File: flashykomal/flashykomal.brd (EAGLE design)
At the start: 54.6 x 58.4 mm, 29 parts, among them IC1 MEGA8-P, IC2 LM358, IC3 LM2397

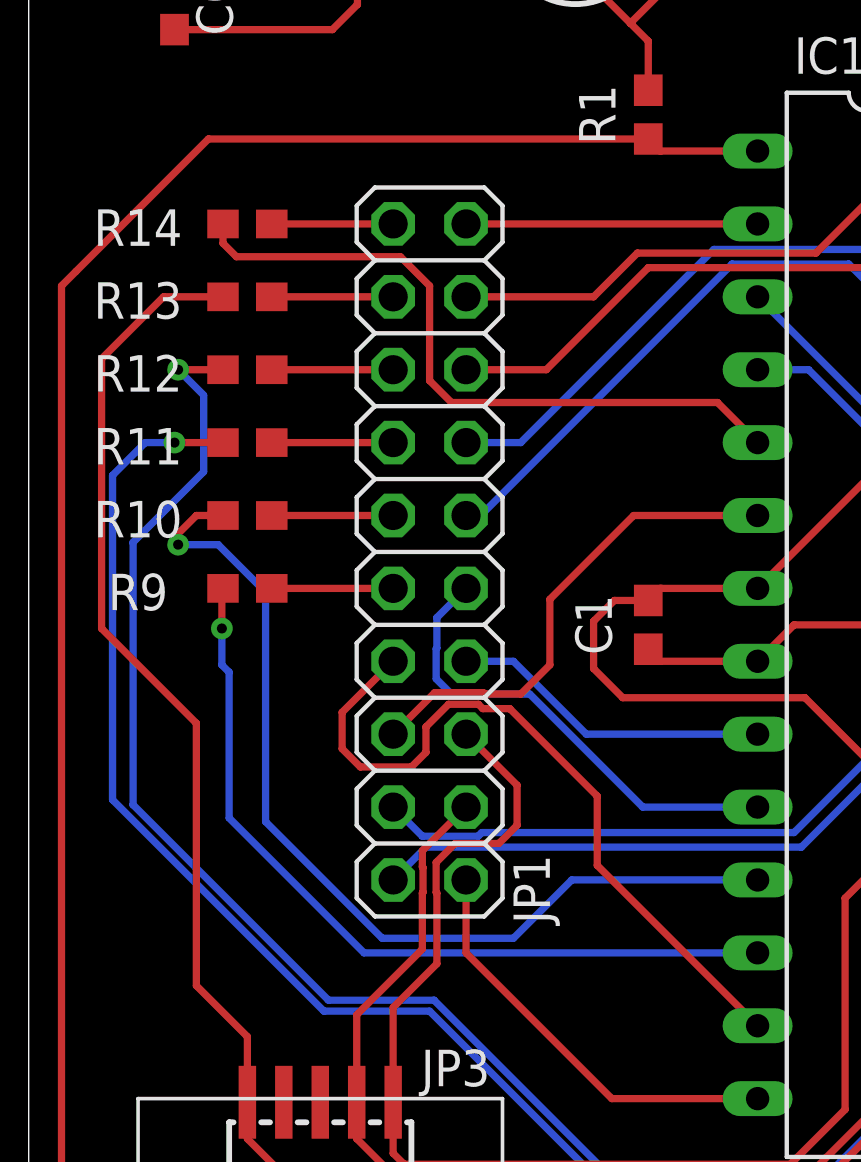
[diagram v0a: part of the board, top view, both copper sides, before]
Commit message: Add JP1 markings
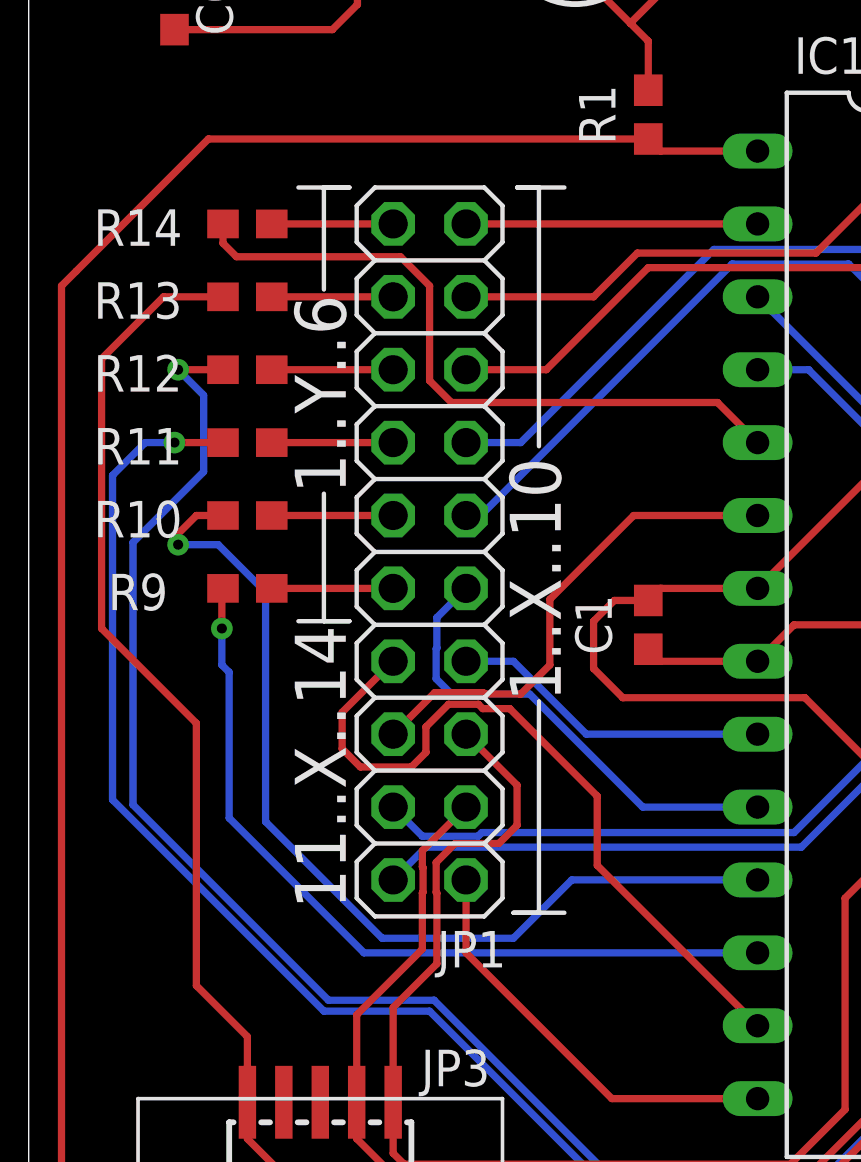
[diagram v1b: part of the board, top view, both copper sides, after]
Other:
- board text added: "1..X..10"
- board text added: "1..Y..6"
- board text added: "11..X..14"
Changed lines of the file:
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@@
 <?xml version="1.0" encoding="utf-8"?>
 <!DOCTYPE eagle SYSTEM "eagle.dtd">
-<eagle version="9.4.2">
+<eagle version="9.1.3">
 <drawing>
 <settings>
@@
 <text x="24.13" y="48.26" size="1.27" layer="25" ratio="15">VIN</text>
 <text x="31.75" y="48.26" size="1.27" layer="25" ratio="15">GND</text>
+<text x="18.542" y="22.733" size="1.778" layer="25" rot="R90">1..X..10</text>
+<text x="11.049" y="15.494" size="1.778" layer="25" rot="R90">11..X..14</text>
+<text x="11.049" y="29.972" size="1.778" layer="25" rot="R90">1..Y..6</text>
+<wire x1="10.287" y1="29.972" x2="10.287" y2="25.527" width="0.1524" layer="25"/>
+<wire x1="10.287" y1="25.527" x2="11.176" y2="25.527" width="0.1524" layer="25"/>
+<wire x1="11.176" y1="25.527" x2="9.398" y2="25.527" width="0.1524" layer="25"/>
+<wire x1="10.287" y1="37.084" x2="10.287" y2="40.64" width="0.1524" layer="25"/>
+<wire x1="10.287" y1="40.64" x2="11.176" y2="40.64" width="0.1524" layer="25"/>
+<wire x1="11.176" y1="40.64" x2="9.398" y2="40.64" width="0.1524" layer="25"/>
+<wire x1="17.78" y1="31.623" x2="17.78" y2="40.64" width="0.1524" layer="25"/>
+<wire x1="17.78" y1="40.64" x2="17.018" y2="40.64" width="0.1524" layer="25"/>
+<wire x1="17.018" y1="40.64" x2="18.669" y2="40.64" width="0.1524" layer="25"/>
+<wire x1="17.78" y1="22.733" x2="17.78" y2="15.367" width="0.1524" layer="25"/>
+<wire x1="17.78" y1="15.367" x2="16.891" y2="15.367" width="0.1524" layer="25"/>
+<wire x1="16.891" y1="15.367" x2="18.669" y2="15.367" width="0.1524" layer="25"/>
 </plain>
 <attributes>
@@
 </element>
 <element name="JP1" library="pinhead" library_urn="urn:adsk.eagle:library:325" package="2X10" package3d_urn="urn:adsk.eagle:package:22405/2" value="" x="13.97" y="27.94" smashed="yes" rot="R90">
-<attribute name="NAME" x="18.161" y="14.986" size="1.27" layer="25" ratio="10" rot="R90"/>
+<attribute name="NAME" x="16.637" y="14.732" size="1.27" layer="25" ratio="10" rot="R180"/>
 <attribute name="VALUE" x="18.415" y="15.24" size="1.27" layer="27" rot="R90"/>
 </element>

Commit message: Power LED
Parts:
- added D1: (no value), SparkFun-LED:LED-0603
- added R15: 330, SparkFun-Resistors:0603
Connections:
- new net N$1: D1.C, R15.2
- net GND: now also R15.1
- net VCC: now also D1.A, JP4.P$2
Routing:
- net VCC: track 151.3 -> 174.7 mm
- net N$1: track 0.00 -> 2.57 mm
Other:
- board text added: "PWR"
- board text added: "VCC"
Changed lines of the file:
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@@
 <wire x1="17.78" y1="15.367" x2="16.891" y2="15.367" width="0.1524" layer="25"/>
 <wire x1="16.891" y1="15.367" x2="18.669" y2="15.367" width="0.1524" layer="25"/>
+<text x="2.159" y="48.768" size="1.27" layer="25" font="vector" ratio="15">PWR</text>
+<text x="27.559" y="48.26" size="1.27" layer="25" ratio="15">VCC</text>
 </plain>
 <attributes>
@@
 </element>
 <element name="JP4" library="atmel-samd" package="PH1X3-381" value="CONN_03" x="29.464" y="50.927" smashed="yes" rot="R180"/>
+<element name="R15" library="SparkFun-Resistors" package="0603" value="330" x="3.81" y="53.34" smashed="yes">
+<attribute name="NAME" x="3.81" y="54.483" size="1.27" layer="25" font="vector" ratio="15" align="bottom-center"/>
+<attribute name="PROD_ID" value="RES-00818" x="3.81" y="53.34" size="1.778" layer="27" display="off"/>
+<attribute name="VALUE" x="3.81" y="52.578" size="0.6096" layer="27" font="vector" ratio="20" align="top-center"/>
+</element>
+<element name="D1" library="SparkFun-LED" package="LED-0603" value="" x="3.81" y="50.8" smashed="yes">
+<attribute name="NAME" x="6.604" y="50.165" size="1.27" layer="25" font="vector" ratio="15" align="bottom-center"/>
+<attribute name="VALUE" x="3.81" y="50.165" size="0.6096" layer="27" font="vector" ratio="20" align="top-center"/>
+</element>
 </elements>
 <signals>
@@
 </polygon>
 <contactref element="JP4" pad="P$1"/>
+<contactref element="R15" pad="1"/>
 </signal>
 <signal name="N$2">
@@
 <wire x1="21.59" y1="45.74" x2="21.59" y2="44.03" width="0.254" layer="1"/>
 <wire x1="20.965" y1="46.365" x2="22.86" y2="48.26" width="0.254" layer="1"/>
-<wire x1="22.86" y1="48.26" x2="34.925" y2="48.26" width="0.254" layer="1"/>
+<wire x1="22.86" y1="48.26" x2="29.464" y2="48.26" width="0.254" layer="1"/>
+<wire x1="29.464" y1="48.26" x2="34.925" y2="48.26" width="0.254" layer="1"/>
 <wire x1="34.925" y1="48.26" x2="36.83" y2="48.26" width="0.254" layer="1"/>
 <wire x1="48.26" y1="32.17" x2="46.316" y2="32.17" width="0.254" layer="1"/>
@@
 <wire x1="12.573" y1="1.524" x2="31.75" y2="1.524" width="0.254" layer="1"/>
 <wire x1="31.75" y1="1.524" x2="38.1" y2="7.874" width="0.254" layer="1"/>
+<contactref element="JP4" pad="P$2"/>
+<wire x1="29.464" y1="50.927" x2="29.464" y2="48.26" width="0.254" layer="1"/>
+<contactref element="D1" pad="A"/>
+<wire x1="2.933" y1="50.8" x2="2.933" y2="44.946" width="0.254" layer="1"/>
+<wire x1="2.933" y1="44.946" x2="3.683" y2="44.196" width="0.254" layer="1"/>
+<wire x1="13.7414" y1="45.8724" x2="13.7414" y2="48.9204" width="0.254" layer="1"/>
+<wire x1="3.683" y1="44.196" x2="12.065" y2="44.196" width="0.254" layer="1"/>
+<wire x1="12.065" y1="44.196" x2="13.7414" y2="45.8724" width="0.254" layer="1"/>
 </signal>
 <signal name="AVCC">
@@
 <wire x1="17.272" y1="53.213" x2="23.368" y2="53.213" width="0.254" layer="1"/>
 </signal>
+<signal name="N$1">
+<contactref element="R15" pad="2"/>
+<contactref element="D1" pad="C"/>
+<wire x1="4.66" y1="53.34" x2="4.66" y2="50.8" width="0.254" layer="1"/>
+<wire x1="4.66" y1="50.8" x2="4.687" y2="50.8" width="0.254" layer="1"/>
+</signal>
 </signals>
